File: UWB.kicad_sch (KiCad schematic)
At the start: 23 parts, among them Q2 Q_NMOS, Q3 Q_NMOS, U2 DW3210, U4 ATX-13

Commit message: schematic capture like half done, need to do a lot of the smaller things
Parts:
- added FB2: TBD, symbol Device:FerriteBead_Small
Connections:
- net +3.3V is gone; now on net +1V8: D1.2 (A), D2.2 (A)
- net GND: now also FB2.2; no longer R1.1, U2.10 (RF_GND), U2.11 (RF_GND), U2.12 (RF_GND), U2.14 (RF_GND), U2.15 (RF_GND), U2.16 (RF_GND), U2.17 (RF_GND), U2.19 (RF_GND), U2.20 (RF_GND)
- net DW_EXTON: now reaches U2.31 (EXTON)
- net MSIO renamed MISO
- new net: FB2.1, R1.1, U2.10 (RF_GND), U2.11 (RF_GND), U2.12 (RF_GND), U2.14 (RF_GND), U2.15 (RF_GND), U2.16 (RF_GND), U2.17 (RF_GND), U2.19 (RF_GND), U2.20 (RF_GND)
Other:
- note added: "LL - SPI Mode 0"
- note added: "TO:DO: - TX/RX LED component selection - RFFE implementation - UWB antenna - Ferrite bead component selection - Test pads"
- note removed: "SPI Mode 0"
- note removed: "TO:DO: - TX/RX LED component selection"

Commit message: all schematic done but RF
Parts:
- removed Q2, Q3: Q_NMOS, symbol Device:Q_NMOS
- added JP2: RF_GND_BRIDGE, symbol Jumper:SolderJumper_2_Bridged
- added Q1: NMOS, Package_TO_SOT_SMD:SOT-363_SC-70-6, symbol Transistor_FET:Q_Dual_NMOS_S1G1D2S2G2D1
- added TP24: DW_WAKEUP, symbol Connector:TestPoint
- added TP25: DW_RST, symbol Connector:TestPoint
- added TP26: DW_IRQ, symbol Connector:TestPoint
- added TP27: RX, symbol Connector:TestPoint
- added TP28: TX, symbol Connector:TestPoint
- added TP29: SYNC, symbol Connector:TestPoint
- added TP8: DW_EXTON, symbol Connector:TestPoint
- C20, C21, C22, C24, C25, C27, C28, C29, C30: footprint (none) -> Capacitor_SMD:C_0402_1005Metric
- C23, C26: footprint (none) -> Capacitor_SMD:C_0603_1608Metric
- D1: value RX -> RX,Orange; footprint (none) -> LED_SMD:LED_0603_1608Metric
- D2: value TX -> TX,White; footprint (none) -> LED_SMD:LED_0603_1608Metric
- FB1: value TBD -> BLM15PX330SZ1D; footprint (none) -> Inductor_SMD:L_0603_1608Metric
- FB2: now not fitted
- R1: value 50 -> 50R0; footprint (none) -> Resistor_SMD:R_0402_1005Metric
- R2, R3: footprint (none) -> Resistor_SMD:R_0603_1608Metric
- R4, R5: value TBD -> 330; footprint (none) -> Resistor_SMD:R_0603_1608Metric
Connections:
- net +1V8: no longer D1.2 (A), D2.2 (A)
- net DW_EXTON: now also TP8.1
- net DW_IRQ: now also TP26.1
- net DW_RST: now also TP25.1
- net DW_WAKEUP: now also TP24.1
- net GND: now also JP2.2 (B), Q1.1 (S), Q1.4 (S)
- net RXLED: now also Q1.2 (G), TP27.1
- net SYNC: now also TP29.1
- net TXLED: now also Q1.5 (G), TP28.1
- net at R5.2: now also Q1.3 (D)
- net at R4.2: now also Q1.6 (D)
- net RF_UWB_GND: now reaches FB2.1, R1.1, U2.10 (RF_GND), U2.11 (RF_GND), U2.12 (RF_GND), U2.14 (RF_GND), U2.15 (RF_GND), U2.16 (RF_GND), U2.17 (RF_GND), U2.19 (RF_GND), U2.20 (RF_GND)
- net RF_UWB_GND: now also JP2.1 (A)
- net RF_UWB: now reaches U2.18 (RF1)
- new net VSYS: D1.2 (A), D2.2 (A)
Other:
- note added: "TO:DO: - RFFE implementation - UWB antenna"
- note added: "UWB - ???G"
- note removed: "TO:DO: - TX/RX LED component selection - RFFE implementation - UWB antenna - Ferrite bead component selection - Test pads"
- moved on the sheet: R1

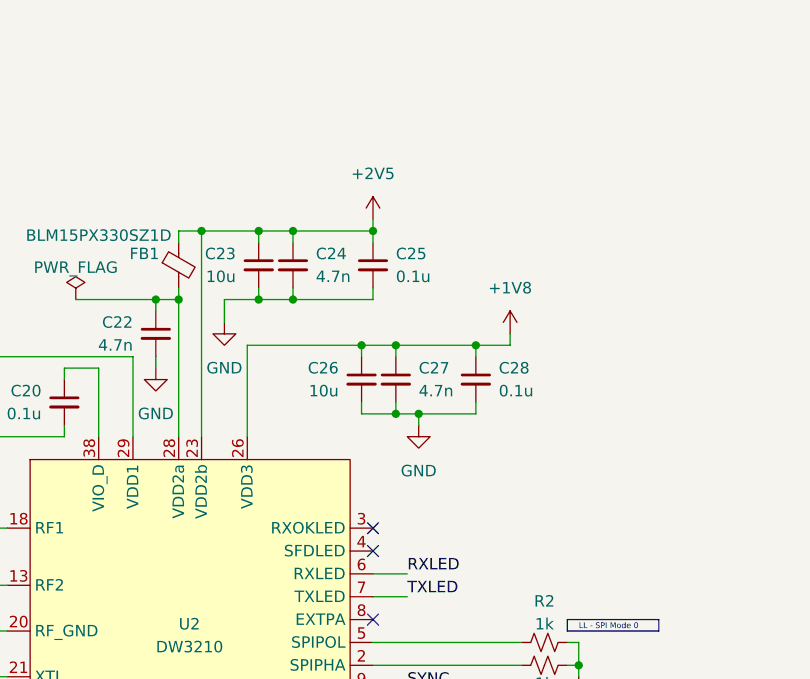
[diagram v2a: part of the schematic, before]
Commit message: schematic & bom done except for UWB RF
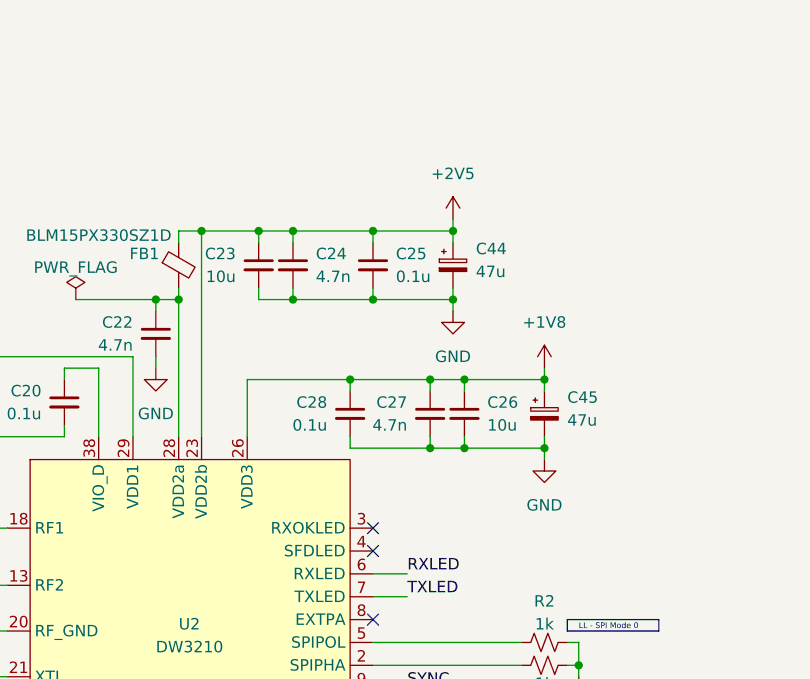
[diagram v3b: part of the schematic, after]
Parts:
- added C44, C45: 47u, Capacitor_SMD:CP_Elec_5x5.8, symbol Device:C_Polarized_Small
- FB2: footprint (none) -> Inductor_SMD:L_0603_1608Metric
- JP2: footprint (none) -> Jumper:SolderJumper-2_P1.3mm_Bridged2Bar_RoundedPad1.0x1.5mm
- TP24, TP25, TP26, TP27, TP28, TP29, TP8: footprint (none) -> TestPoint:TestPoint_Pad_D1.5mm
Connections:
- net +1V8: now also C45.1
- net +2V5: now also C44.1
- net GND: now also C44.2, C45.2
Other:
- moved on the sheet: C26, C27

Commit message: routing started
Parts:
- added C40: 2.0p, Capacitor_SMD:C_0402_1005Metric, symbol Device:C_Small
- added C43: 0.22u, Capacitor_SMD:C_0402_1005Metric, symbol Device:C_Small
- added R16, R17: 10k, Resistor_SMD:R_0402_1005Metric, symbol Device:R_Small_US
- R2, R3, R4, R5: footprint Resistor_SMD:R_0603_1608Metric -> Resistor_SMD:R_0402_1005Metric
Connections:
- net GND: now also C43.2, R16.1, R17.1
- net RF_UWB: now also C40.1
- net RXLED: now also R16.2
- net TXLED: now also R17.2
- new net: C43.1, U2.27 (VTX_D)
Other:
- moved on the sheet: C26, C27, C28, C45, D1, D2, Q1A, Q1B, R4, R5

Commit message: routing hell
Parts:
- removed FB2: TBD, Inductor_SMD:L_0603_1608Metric, symbol Device:FerriteBead_Small
- removed JP2: RF_GND_BRIDGE, Jumper:SolderJumper-2_P1.3mm_Bridged2Bar_RoundedPad1.0x1.5mm, symbol Jumper:SolderJumper_2_Bridged
- added AE3: ACR0301U, Inductor_SMD:L_1206_3216Metric, symbol Device:Antenna_Chip
- added Z1, Z3: OC, Inductor_SMD:L_0402_1005Metric, symbol Device:R
- added Z2: 0R, Inductor_SMD:L_0402_1005Metric, symbol Device:R
- TP24, TP25, TP26, TP27, TP28, TP29, TP8: footprint TestPoint:TestPoint_Pad_D1.5mm -> TestPoint:TestPoint_Pad_D1.0mm
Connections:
- net RF_UWB_GND is gone; now on net GND: R1.1, U2.10 (RF_GND), U2.11 (RF_GND), U2.12 (RF_GND), U2.14 (RF_GND), U2.15 (RF_GND), U2.16 (RF_GND), U2.17 (RF_GND), U2.19 (RF_GND), U2.20 (RF_GND)
- net GND: now also Z1.2, Z3.2
- net at C40.2: now also Z1.1, Z2.2
- new net: AE3.2 (PCB_Trace), Z2.1, Z3.1
- no-connect marks 4 -> 5
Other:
- note added: "TO:DO:"
- note added: "UWB - 6.5/7.9G"
- note added: "WILL NEED TUNING"
- note removed: "TO:DO: - RFFE implementation - UWB antenna"
- note removed: "UWB - ???G"
- moved on the sheet: C40

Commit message: ready for DR
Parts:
- AE3: footprint Inductor_SMD:L_1206_3216Metric -> TrActor:ACR0301U
- C44, C45: value 47u -> 22u; footprint Capacitor_SMD:CP_Elec_5x5.8 -> Capacitor_SMD:CP_Elec_4x5.4
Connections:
- net UWB_ANT: now reaches AE3.2 (PCB_Trace), Z2.1, Z3.1
- net RF_UWB_AC: now reaches C40.2, Z1.1, Z2.2
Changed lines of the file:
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@@
 	)
 	(junction
+		(at 119.38 58.42)
+		(diameter 0)
+		(color 0 0 0 0)
+	)
+	(junction
 		(at 83.82 73.66)
 		(diameter 0)
@@
 	)
 	(junction
-		(at 242.57 57.15)
+		(at 128.27 58.42)
 		(diameter 0)
 		(color 0 0 0 0)
 	)
 	(junction
-		(at 109.22 50.8)
+		(at 242.57 57.15)
 		(diameter 0)
 		(color 0 0 0 0)
 	)
 	(junction
-		(at 119.38 50.8)
+		(at 109.22 50.8)
 		(diameter 0)
 		(color 0 0 0 0)
 	)
 	(junction
-		(at 243.84 113.03)
+		(at 119.38 50.8)
 		(diameter 0)
 		(color 0 0 0 0)
 	)
 	(junction
-		(at 119.38 58.42)
+		(at 243.84 113.03)
 		(diameter 0)
 		(color 0 0 0 0)
@@
 	)
 	(junction
-		(at 128.27 58.42)
-		(diameter 0)
-		(color 0 0 0 0)
-	)
-	(junction
 		(at 140.97 109.22)
 		(diameter 0)
@@
 	(wire
 		(pts
-			(xy 115.57 58.42) (xy 137.16 58.42)
+			(xy 115.57 58.42) (xy 119.38 58.42)
 		)
 		(stroke
@@
 	(wire
 		(pts
+			(xy 128.27 58.42) (xy 137.16 58.42)
+		)
+		(stroke
+			(width 0)
+			(type default)
+		)
+	)
+	(wire
+		(pts
+			(xy 119.38 57.15) (xy 119.38 58.42)
+		)
+		(stroke
+			(width 0)
+			(type default)
+		)
+	)
+	(wire
+		(pts
 			(xy 273.05 48.26) (xy 273.05 49.53)
 		)
@@
 	(wire
 		(pts
+			(xy 119.38 58.42) (xy 128.27 58.42)
+		)
+		(stroke
+			(width 0)
+			(type default)
+		)
+	)
+	(wire
+		(pts
 			(xy 242.57 30.48) (xy 242.57 34.29)
 		)
@@
 	(wire
 		(pts
-			(xy 128.27 57.15) (xy 128.27 58.42)
-		)
-		(stroke
-			(width 0)
-			(type default)
-		)
-	)
-	(wire
-		(pts
 			(xy 106.68 52.07) (xy 106.68 50.8)
 		)
@@
 	(wire
 		(pts
-			(xy 119.38 57.15) (xy 119.38 58.42)
+			(xy 116.84 132.08) (xy 111.76 132.08)
 		)
 		(stroke
@@
 	(wire
 		(pts
-			(xy 116.84 132.08) (xy 111.76 132.08)
+			(xy 128.27 57.15) (xy 128.27 58.42)
 		)
 		(stroke
@@
 		)
 	)
+	(label "UWB_ANT"
+		(at 256.54 113.03 0)
+		(effects
+			(font
+				(size 1.27 1.27)
+			)
+			(justify left bottom)
+		)
+	)
 	(label "SYNC"
 		(at 228.6 29.21 270)
@@
 		)
 	)
+	(label "RF_UWB_AC"
+		(at 236.22 113.03 0)
+		(effects
+			(font
+				(size 1.27 1.27)
+			)
+			(justify left bottom)
+		)
+	)
 	(label "CLK_38.4M"
 		(at 270.51 82.55 0)
@@
 		)
 		(property "Netclass" "RF"
-			(at 280.0604 102.87 0)
+			(at 281.2796 102.87 0)
 			(show_name no)
 			(do_not_autoplace no)
@@
 					(size 1.27 1.27)
 				)
-				(justify right)
+				(justify left)
 			)
 		)
@@
 			)
 		)
-		(property "Footprint" "Inductor_SMD:L_1206_3216Metric"
+		(property "Footprint" "TrActor:ACR0301U"
 			(at 274.955 118.11 0)
 			(hide yes)
@@
 			)
 		)
-		(property "Datasheet" ""
+		(property "Datasheet" "https://abracon.com/datasheets/ACR0301U.pdf"
 			(at 274.955 118.11 0)
 			(hide yes)
@@
 			)
 		)
-		(property "Value" "47u"
+		(property "Value" "22u"
 			(at 158.75 71.8438 0)
 			(show_name no)
@@
 			)
 		)
-		(property "Footprint" "Capacitor_SMD:CP_Elec_5x5.8"
+		(property "Footprint" "Capacitor_SMD:CP_Elec_4x5.4"
 			(at 156.21 71.12 0)
 			(hide yes)
@@
 			)
 		)
-		(property "Value" "47u"
+		(property "Value" "22u"
 			(at 139.7 55.3338 0)
 			(show_name no)
@@
 			)
 		)
-		(property "Footprint" "Capacitor_SMD:CP_Elec_5x5.8"
+		(property "Footprint" "Capacitor_SMD:CP_Elec_4x5.4"
 			(at 137.16 54.61 0)
 			(hide yes)

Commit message: ordering commit fr
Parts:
- FB1: footprint Inductor_SMD:L_0603_1608Metric -> Inductor_SMD:L_0402_1005Metric
- TP24, TP25, TP26, TP27, TP28, TP29, TP8, Z1, Z3: now left out of the parts list
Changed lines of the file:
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@@
 		(body_style 1)
 		(exclude_from_sim no)
-		(in_bom yes)
+		(in_bom no)
 		(on_board yes)
 		(in_pos_files yes)
@@
 			)
 		)
-		(property "Footprint" "Inductor_SMD:L_0603_1608Metric"
+		(property "Footprint" "Inductor_SMD:L_0402_1005Metric"
 			(at 104.902 54.61 90)
 			(hide yes)
@@
 		(body_style 1)
 		(exclude_from_sim no)
-		(in_bom yes)
+		(in_bom no)
 		(on_board yes)
 		(in_pos_files yes)
@@
 		(body_style 1)
 		(exclude_from_sim no)
-		(in_bom yes)
+		(in_bom no)
 		(on_board yes)
 		(in_pos_files yes)
@@
 		(body_style 1)
 		(exclude_from_sim no)
-		(in_bom yes)
+		(in_bom no)
 		(on_board yes)
 		(in_pos_files yes)
@@
 		(body_style 1)
 		(exclude_from_sim no)
-		(in_bom yes)
+		(in_bom no)
 		(on_board yes)
 		(in_pos_files yes)
@@
 		(body_style 1)
 		(exclude_from_sim no)
-		(in_bom yes)
+		(in_bom no)
 		(on_board yes)
 		(in_pos_files yes)
@@
 		(body_style 1)
 		(exclude_from_sim no)
-		(in_bom yes)
+		(in_bom no)
 		(on_board yes)
 		(in_pos_files yes)
@@
 		(body_style 1)
 		(exclude_from_sim no)
-		(in_bom yes)
+		(in_bom no)
 		(on_board yes)
 		(in_pos_files yes)
@@
 		(body_style 1)
 		(exclude_from_sim no)
-		(in_bom yes)
+		(in_bom no)
 		(on_board yes)
 		(in_pos_files yes)
